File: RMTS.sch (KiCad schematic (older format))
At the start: 54 parts, among them J1 USB_B, J10 CONN_02, J2 Programmer, J3 Screw_Terminal_01x03, J4 Screw_Terminal_01x04, J5 Screw_Terminal_01x02, J6 Screw_Terminal_01x02, J7 Micro_SD_Card_Det_Hirose_DM3AT, J8 CONN_03, J9 CONN_02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

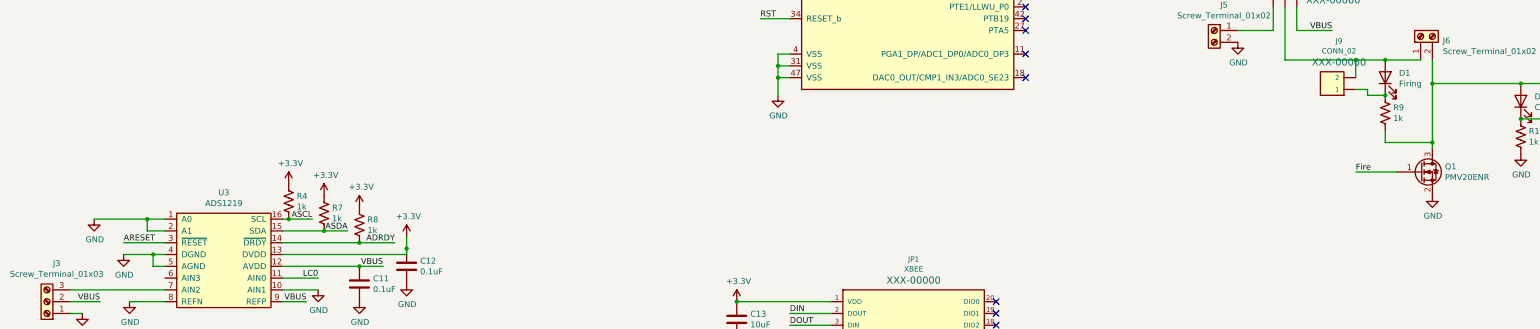
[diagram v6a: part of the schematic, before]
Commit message: Pulled ADC enable high, added diode to firing circuit, rerouted some traces
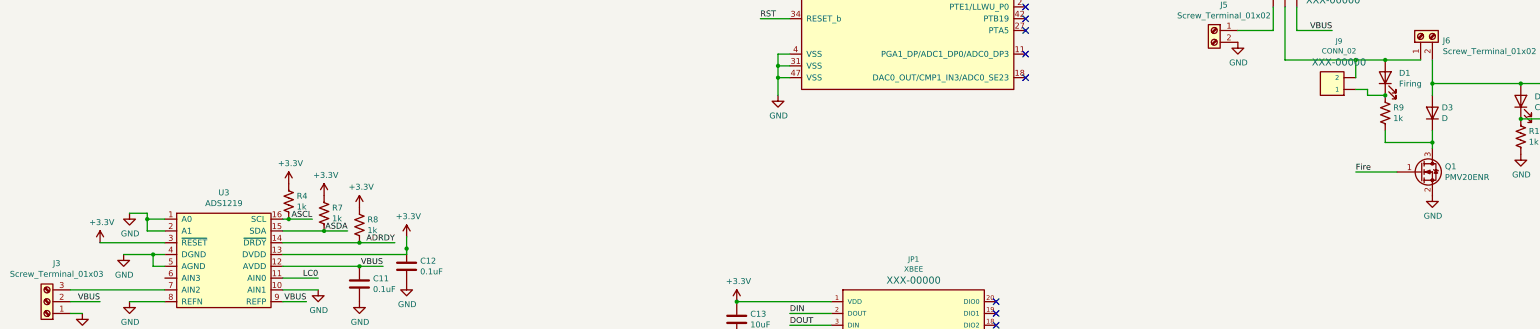
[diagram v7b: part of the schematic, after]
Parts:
- added D3: D, Diode_SMD:D_SOD-123, symbol Device:D
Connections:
- net ARESET is gone; now on net +3V3: U3.3 (~RESET)
- net at D2.2 (A), J10.1, J6.2 (Pin_2): now also D3.2 (A); no longer Q1.3 (D), R9.2
- new net: D3.1 (K), Q1.3 (D), R9.2
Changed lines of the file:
@@
 $EndComp
-Wire Wire Line
-	3150 7000 2800 7000
-Text Label 2800 7000 0    50   ~ 0
-ARESET
 Wire Wire Line
 	3150 7200 3050 7200
@@
 L power:GND #PWR0133
 U 1 1 5D440F40
-P 2550 6800
-F 0 "#PWR0133" H 2550 6550 50  0001 C CNN
-F 1 "GND" H 2555 6627 50  0000 C CNN
-F 2 "" H 2550 6800 50  0001 C CNN
-F 3 "" H 2550 6800 50  0001 C CNN
-	1    2550 6800
-	1    0    0    -1
-$EndComp
-Wire Wire Line
-	2550 6800 3000 6800
+P 2850 6750
+F 0 "#PWR0133" H 2850 6500 50  0001 C CNN
+F 1 "GND" H 2855 6577 50  0000 C CNN
+F 2 "" H 2850 6750 50  0001 C CNN
+F 3 "" H 2850 6750 50  0001 C CNN
+	1    2850 6750
+	1    0    0    -1
+$EndComp
 Wire Wire Line
 	3150 6900 3000 6900
 Wire Wire Line
 	3000 6900 3000 6800
-Connection ~ 3000 6800
 Wire Wire Line
 	3000 6800 3150 6800
@@
 Wire Wire Line
 	14650 5650 13900 5650
-Connection ~ 13900 5650
 $Comp
 L Device:LED D1
@@
 	13500 6150 13900 6150
 Wire Wire Line
-	13900 5650 13900 6150
-Wire Wire Line
 	13900 6150 13900 6200
-Connection ~ 13900 6150
 Wire Wire Line
 	13600 6400 13250 6400
@@
 Wire Wire Line
 	4150 7500 4350 7500
+$Comp
+L Device:D D3
+U 1 1 5D761E8A
+P 13900 5900
+F 0 "D3" V 13946 5821 50  0000 R CNN
+F 1 "D" V 13855 5821 50  0000 R CNN
+F 2 "Diode_SMD:D_SOD-123" H 13900 5900 50  0001 C CNN
+F 3 "~" H 13900 5900 50  0001 C CNN
+	1    13900 5900
+	0    -1   -1   0
+$EndComp
+Wire Wire Line
+	13900 5650 13900 5750
+Connection ~ 13900 5650
+Wire Wire Line
+	13900 6050 13900 6150
+Connection ~ 13900 6150
+Wire Wire Line
+	3000 6800 3000 6750
+Wire Wire Line
+	3000 6750 2850 6750
+Connection ~ 3000 6800
+$Comp
+L power:+3.3V #PWR0143
+U 1 1 5D78AE26
+P 2600 7000
+F 0 "#PWR0143" H 2600 6850 50  0001 C CNN
+F 1 "+3.3V" H 2615 7173 50  0000 C CNN
+F 2 "" H 2600 7000 50  0001 C CNN
+F 3 "" H 2600 7000 50  0001 C CNN
+	1    2600 7000
+	1    0    0    -1
+$EndComp
+Wire Wire Line
+	2600 7000 3150 7000
 $EndSCHEMATC

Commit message: Removed backup crystal, resized board
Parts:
- removed Y2: Crystal_GND24_Small, Crystal:Crystal_SMD_3225-4Pin_3.2x2.5mm, symbol Device:Crystal_GND24_Small
- J10, J9: symbol SparkFun-Connectors:CONN_02 -> RMTS-rescue:CONN_02-SparkFun-Connectors
- J8: symbol SparkFun-Connectors:CONN_03 -> RMTS-rescue:CONN_03-SparkFun-Connectors
- JP1: symbol SparkFun-RF:XBEE -> RMTS-rescue:XBEE-SparkFun-RF
- U2: symbol Mine:MK20DX256VLH7 -> RMTS-rescue:MK20DX256VLH7-Mine
- U3: symbol Mine:ADS1219 -> RMTS-rescue:ADS1219-Mine
- U4: symbol Mine:MCP6N11 -> RMTS-rescue:MCP6N11-Mine
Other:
- note removed: "Backup Crystal"
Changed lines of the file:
@@
 EESchema Schematic File Version 4
 LIBS:RMTS-cache
-EELAYER 29 0
+EELAYER 30 0
 EELAYER END
 $Descr A3 16535 11693
@@
 $EndDescr
 $Comp
-L Mine:MK20DX256VLH7 U2
+L RMTS-rescue:MK20DX256VLH7-Mine U2
 U 1 1 5D344F89
 P 9450 1500
@@
 Connection ~ 6800 4100
 $Comp
-L Mine:ADS1219 U3
+L RMTS-rescue:ADS1219-Mine U3
 U 1 1 5D3AE65D
 P 3650 6800
@@
 $EndComp
 $Comp
-L Mine:MCP6N11 U4
+L RMTS-rescue:MCP6N11-Mine U4
 U 1 1 5D4392E2
 P 3650 8100
@@
 	4150 7400 4450 7400
 $Comp
-L SparkFun-RF:XBEE JP1
+L RMTS-rescue:XBEE-SparkFun-RF JP1
 U 1 1 5D38660F
 P 9500 7900
@@
 $EndComp
 $Comp
-L SparkFun-Connectors:CONN_03 J8
+L RMTS-rescue:CONN_03-SparkFun-Connectors J8
 U 1 1 5D6FAE37
 P 12550 4900
@@
 Text Label 8200 3750 0    50   ~ 0
 XTAL2
-Wire Wire Line
-	5400 3450 5850 3450
-Wire Wire Line
-	5850 3750 5400 3750
-Text Label 5850 3450 2    50   ~ 0
-XTAL1
-Text Label 5850 3750 2    50   ~ 0
-XTAL2
-$Comp
-L Device:Crystal_GND24_Small Y2
-U 1 1 5D4A38E4
-P 5400 3600
-F 0 "Y2" V 5350 3750 50  0000 L CNN
-F 1 "Crystal_GND24_Small" V 5400 3750 50  0000 L CNN
-F 2 "Crystal:Crystal_SMD_3225-4Pin_3.2x2.5mm" H 5400 3600 50  0001 C CNN
-F 3 "~" H 5400 3600 50  0001 C CNN
-	1    5400 3600
-	0    1    1    0
-$EndComp
-Wire Wire Line
-	5400 3500 5400 3450
-Wire Wire Line
-	5400 3700 5400 3750
-$Comp
-L power:GND #PWR0132
-U 1 1 5D4B952D
-P 5550 3850
-F 0 "#PWR0132" H 5550 3600 50  0001 C CNN
-F 1 "GND" H 5555 3677 50  0000 C CNN
-F 2 "" H 5550 3850 50  0001 C CNN
-F 3 "" H 5550 3850 50  0001 C CNN
-	1    5550 3850
-	1    0    0    -1
-$EndComp
-Wire Wire Line
-	5500 3600 5550 3600
-Wire Wire Line
-	5550 3600 5550 3800
-Wire Wire Line
-	5550 3800 5250 3800
-Wire Wire Line
-	5250 3800 5250 3600
-Wire Wire Line
-	5250 3600 5300 3600
-Connection ~ 5550 3800
-Wire Wire Line
-	5550 3800 5550 3850
-Text Notes 5300 4200 0    50   ~ 0
-Backup Crystal
 NoConn ~ 13050 1850
 NoConn ~ 13050 2550
@@
 NoConn ~ 10200 8400
 $Comp
-L SparkFun-Connectors:CONN_02 J9
+L RMTS-rescue:CONN_02-SparkFun-Connectors J9
 U 1 1 5D4ED64B
 P 13150 5700
@@
 $EndComp
 $Comp
-L SparkFun-Connectors:CONN_02 J10
+L RMTS-rescue:CONN_02-SparkFun-Connectors J10
 U 1 1 5D4EE378
 P 15300 5650
